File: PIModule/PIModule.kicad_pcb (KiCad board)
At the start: 2 copper layers, 56 x 60 mm, 27 parts, among them J1 SigIn, J2 HVOut, J3 Heater, J4 HeaterOut, J5 HV, J6 SigOut, J7 NFB, J8 PresencePot, U1 ECC83

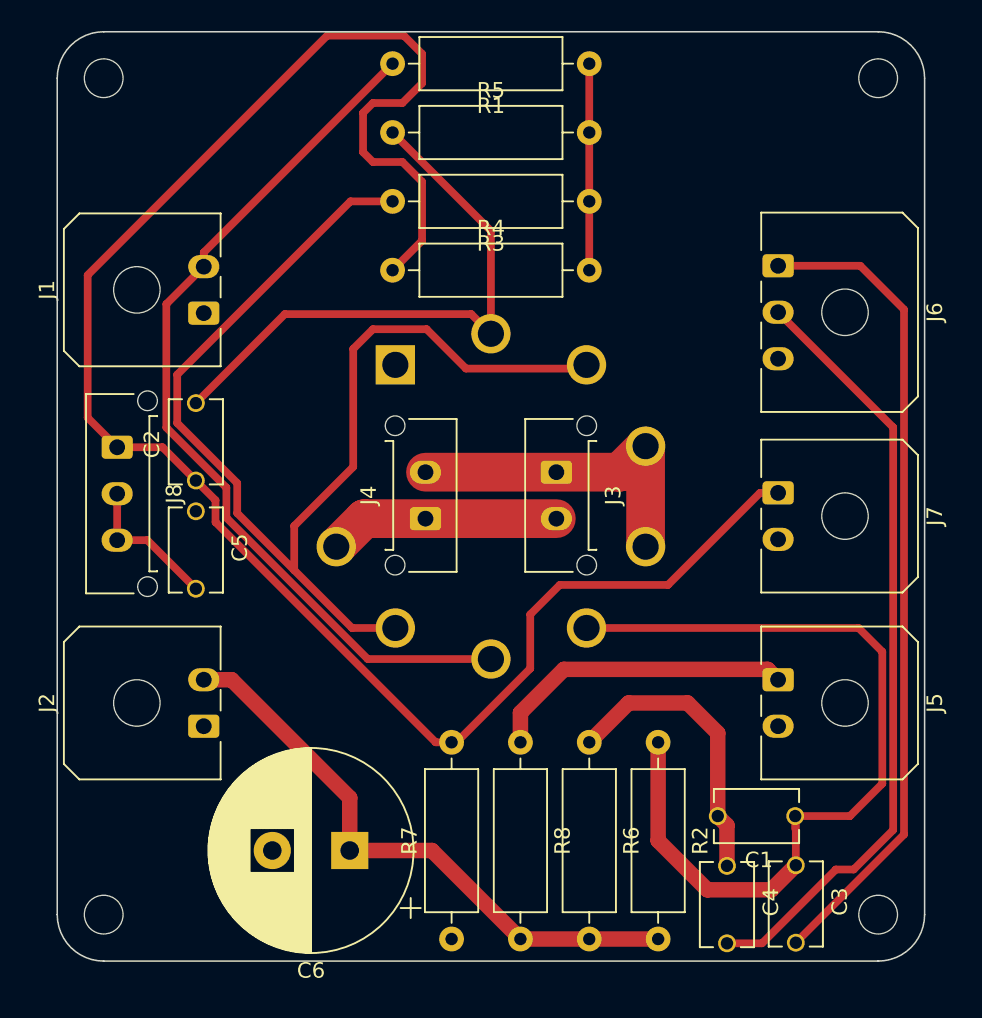
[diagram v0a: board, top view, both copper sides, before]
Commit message: Reroute phase inverter
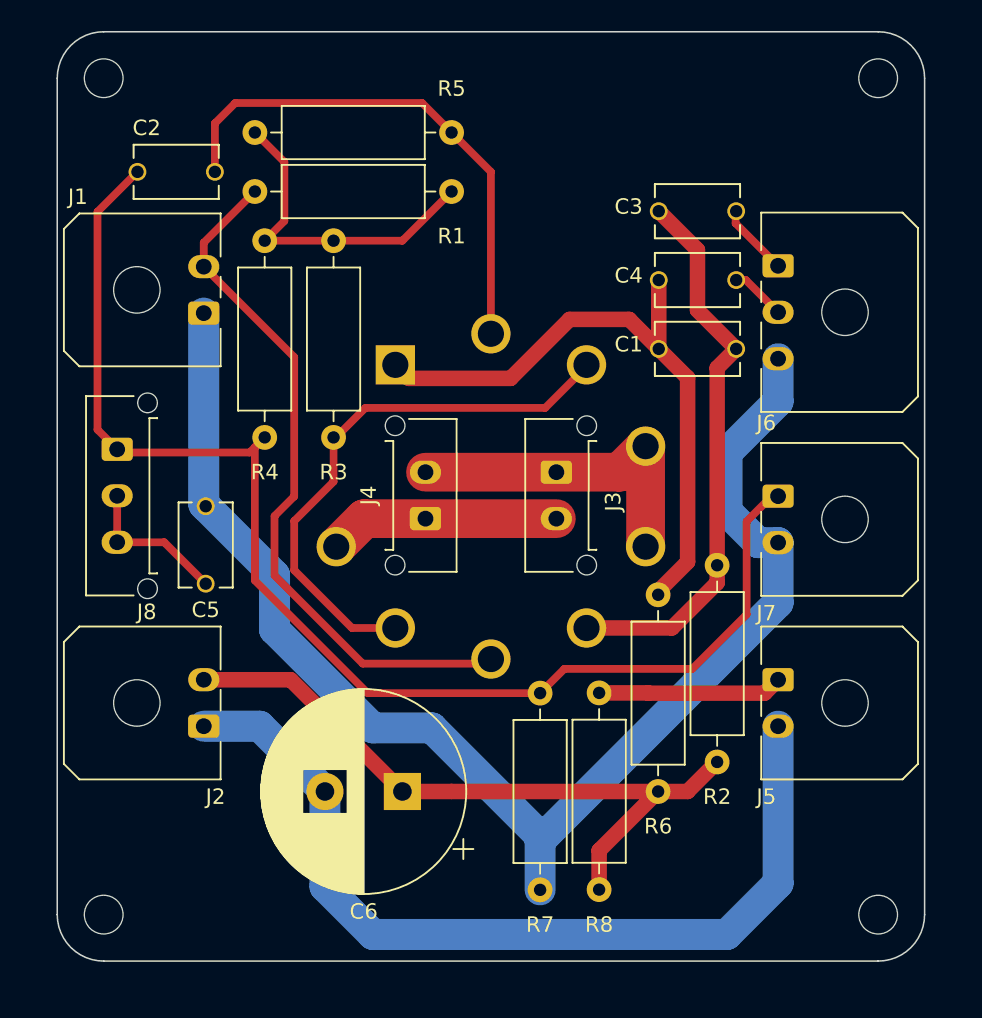
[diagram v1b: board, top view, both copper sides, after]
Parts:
- moved C3 45.2 mm to (172.7, 68.2), turned to 0 degrees
- moved C4 40.4 mm to (172.7, 72.7), turned to 0 degrees
- moved C1 30.4 mm to (172.7, 77.1)
- moved C2 17.5 mm to (139.1, 65.7), turned to 0 degrees
- moved R3 16.7 mm to (149.2, 70.1), turned to -90 degrees
- moved R4 13.6 mm to (144.8, 82.8), turned to 90 degrees
- moved R1 12.1 mm to (156.8, 67.0)
- moved R2 12.0 mm to (174.0, 91.1)
- moved R6 10.5 mm to (170.2, 93.0)
- moved R7 6.54 mm to (162.6, 112.1)
- moved R8 6.00 mm to (166.4, 99.3)
- moved C6 5.11 mm to (153.7, 105.7)
- moved R5 3.81 mm to (156.8, 63.2), turned to 180 degrees
- moved C5 0.71 mm to (141.0, 89.8)
- moved J7 0.21 mm to (177.9, 86.6)
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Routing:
- net GND: track 0.00 -> 89.4 mm
- net GND1: track 0.00 -> 57.8 mm
- net Net-(J6-Pin_1): track 53.1 -> 4.66 mm
- net Net-(J6-Pin_2): track 50.3 -> 3.57 mm
- net Net-(U1A-K): track 74.9 -> 35.8 mm
- net Net-(J7-Pin_1): track 120.9 -> 84.6 mm
- net Net-(U1B-A): track 19.0 -> 41.6 mm
- net Net-(U1A-A): track 56.3 -> 36.2 mm
- net Net-(J1-Pin_2): track 57.8 -> 45.5 mm
- net Net-(R1-Pad1): track 13.3 -> 21.7 mm
- net Net-(J5-Pin_1): track 20.0 -> 11.9 mm
- net HT: track 38.3 -> 44.8 mm
- net Net-(U1B-G): track 37.6 -> 33.8 mm

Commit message: Change connector footprints to contain 3D models. Make necessary PCB modifications to address errors found in the design
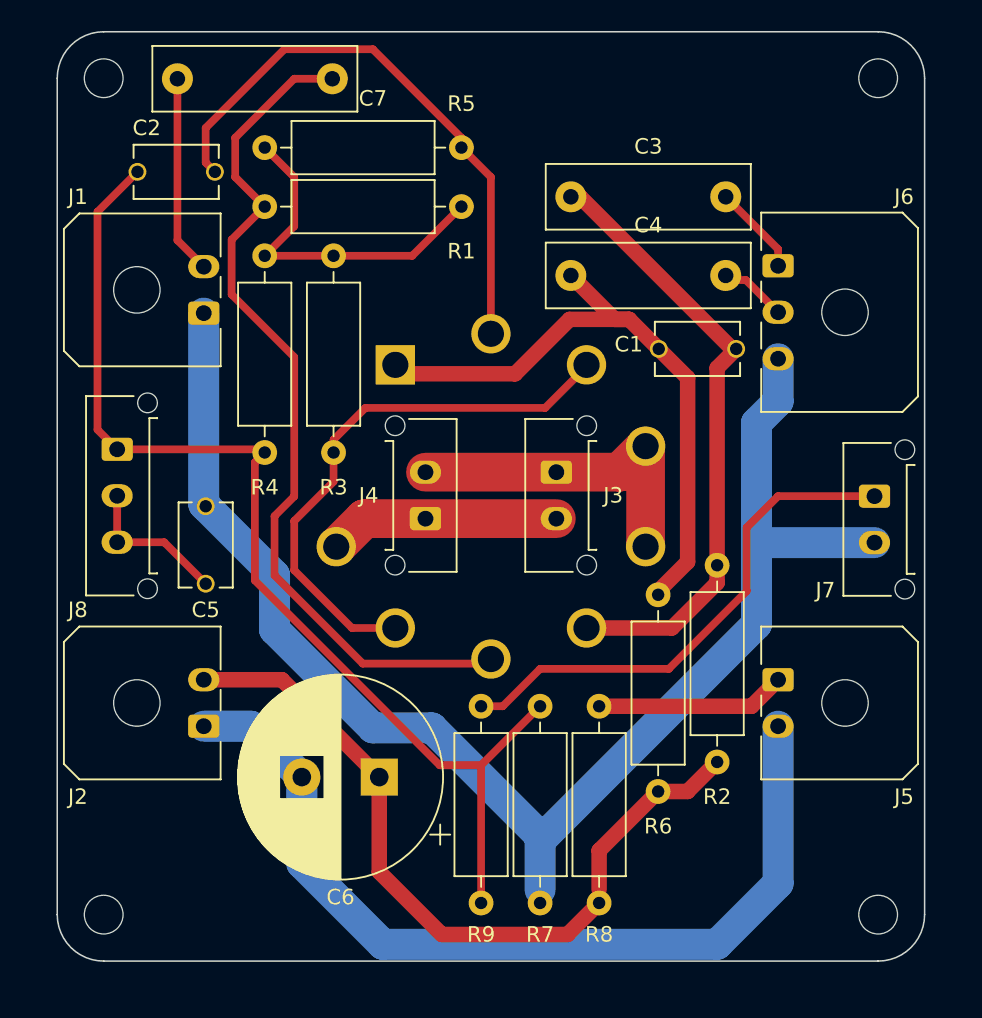
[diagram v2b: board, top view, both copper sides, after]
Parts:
- added C7: 0.022uF, Capacitor_THT:C_Rect_L13.0mm_W4.0mm_P10.00mm_FKS3_FKP3_MKS4, F.Cu at (139.1, 59.7)
- added R9: 100K, Resistor_THT:R_Axial_DIN0309_L9.0mm_D3.2mm_P12.70mm_Horizontal, F.Cu at (158.8, 112.9)
- C3, C4: footprint CustomFootprints:FG26 Cap -> Capacitor_THT:C_Rect_L13.0mm_W4.0mm_P10.00mm_FKS3_FKP3_MKS4
- J1, J2, J5: footprint Connector_Molex:Molex_Micro-Fit_3.0_43650-0200_1x02_P3.00mm_Horizontal -> CustomFootprints:Molex_Micro-Fit_3.0_43650-0200_1x02_P3.00mm_Horizontal
- J3, J4: footprint Connector_Molex:Molex_Micro-Fit_3.0_43650-0215_1x02_P3.00mm_Vertical -> CustomFootprints:Molex_Micro-Fit_3.0_43650-0215_1x02_P3.00mm_Vertical
- J6: footprint Connector_Molex:Molex_Micro-Fit_3.0_43650-0300_1x03_P3.00mm_Horizontal -> CustomFootprints:Molex_Micro-Fit_3.0_43650-0300_1x03_P3.00mm_Horizontal
- J7: footprint Connector_Molex:Molex_Micro-Fit_3.0_43650-0200_1x02_P3.00mm_Horizontal -> CustomFootprints:Molex_Micro-Fit_3.0_43650-0215_1x02_P3.00mm_Vertical
- J8: footprint Connector_Molex:Molex_Micro-Fit_3.0_43650-0315_1x03_P3.00mm_Vertical -> CustomFootprints:Molex_Micro-Fit_3.0_43650-0315_1x03_P3.00mm_Vertical
- moved C3 8.23 mm to (164.5, 67.3)
- moved C4 8.18 mm to (164.5, 72.4)
- moved J7 6.22 mm to (184.2, 86.6)
- moved C6 1.76 mm to (152.2, 104.8)
- moved R5 1.16 mm to (157.5, 64.1)
- moved R1 1.16 mm to (157.5, 67.9)
- moved R3 0.98 mm to (149.2, 71.1)
- moved R4 0.97 mm to (144.8, 83.8)
- moved R8 0.86 mm to (166.4, 100.2)
- moved R7 0.85 mm to (162.6, 112.9)
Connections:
- C2 pad 1: Net-(J7-Pin_1) -> Net-(J8-Pin_1)
- J8 pad 1: Net-(J7-Pin_1) -> Net-(J8-Pin_1)
- R1 pad 2: Net-(J1-Pin_2) -> Net-(U1A-G)
- R4 pad 1: Net-(J7-Pin_1) -> Net-(J8-Pin_1)
- R7 pad 2: Net-(J7-Pin_1) -> Net-(J8-Pin_1)
- U1 pad 7: Net-(J1-Pin_2) -> Net-(U1A-G)
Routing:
- net Net-(J8-Pin_1): track 0.00 -> 71.8 mm
- net Net-(U1A-G): track 0.00 -> 56.4 mm
- net Net-(J7-Pin_1): track 84.6 -> 33.4 mm
- net Net-(J1-Pin_2): track 45.5 -> 12.8 mm
- net HT: track 44.8 -> 49.3 mm
- net GND: track 89.4 -> 93.6 mm
- net Net-(U1A-A): track 36.2 -> 40.0 mm
- net Net-(U1B-G): track 33.8 -> 37.5 mm
- net Net-(J6-Pin_1): track 4.66 -> 5.86 mm
- net Net-(R1-Pad1): track 21.7 -> 22.6 mm

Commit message: Standardized hole size across all boards
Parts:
- removed the REF** at (134.4, 113.7)
- removed the REF** at (184.4, 113.7)
- removed the REF** at (184.4, 59.7)
- removed the REF** at (134.4, 59.7)
- added REF**: MountingHole_2.7mm_M2.5, MountingHole:MountingHole_2.7mm_M2.5, F.Cu at (184.4, 113.7)
- added REF**: MountingHole_2.7mm_M2.5, MountingHole:MountingHole_2.7mm_M2.5, F.Cu at (184.4, 59.7)
- added REF**: MountingHole_2.7mm_M2.5, MountingHole:MountingHole_2.7mm_M2.5, F.Cu at (134.4, 113.7)
- added REF**: MountingHole_2.7mm_M2.5, MountingHole:MountingHole_2.7mm_M2.5, F.Cu at (134.4, 59.7)
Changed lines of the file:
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@@
     )
     (pad_to_mask_clearance 0)
+    (grid_origin 159.385 86.655)
     (pcbplotparams
       (layerselection 0x00010fc_ffffffff)
@@
         (effects (font (size 1 1) (thickness 0.15)))
     )
-    (fp_text value "SigOut" (at 3 3.22 -90) (layer "F.Fab")
+    (fp_text value "SigOut" (at 8.245 -5.59) (layer "F.Fab")
         (effects (font (size 1 1) (thickness 0.15)))
     )
@@
     )
   )
-  (footprint "MountingHole:MountingHole_2.5mm" (layer "F.Cu")
-    (at 134.385 113.655)
-    (descr "Mounting Hole 2.5mm, no annular")
-    (tags "mounting hole 2.5mm no annular")
+  (footprint "MountingHole:MountingHole_2.7mm_M2.5" (layer "F.Cu")
+    (at 184.385 113.655)
+    (descr "Mounting Hole 2.7mm, no annular, M2.5")
+    (tags "mounting hole 2.7mm no annular m2.5")
     (attr exclude_from_pos_files exclude_from_bom)
-    (fp_text reference "REF**" (at 0 -3.5) (layer "F.SilkS") hide
-        (effects (font (size 1 1) (thickness 0.15)))
-    )
-    (fp_text value "MountingHole_2.5mm" (at 0 3.5) (layer "F.Fab") hide
+    (fp_text reference "REF**" (at 0 -3.7) (layer "F.SilkS") hide
+        (effects (font (size 1 1) (thickness 0.15)))
+    )
+    (fp_text value "MountingHole_2.7mm_M2.5" (at 0 3.7) (layer "F.Fab") hide
         (effects (font (size 1 1) (thickness 0.15)))
     )
@@
         (effects (font (size 1 1) (thickness 0.15)))
     )
-    (fp_circle (center 0 0) (end 2.5 0)
+    (fp_circle (center 0 0) (end 2.7 0)
       (stroke (width 0.15) (type solid)) (fill none) (layer "Cmts.User"))
-    (fp_circle (center 0 0) (end 2.75 0)
+    (fp_circle (center 0 0) (end 2.95 0)
       (stroke (width 0.05) (type solid)) (fill none) (layer "F.CrtYd"))
-    (pad "" np_thru_hole circle (at 0 0) (size 2.5 2.5) (drill 2.5) (layers "F&B.Cu" "*.Mask"))
+    (pad "" np_thru_hole circle (at 0 0) (size 2.7 2.7) (drill 2.7) (layers "*.Cu" "*.Mask"))
   )
   (footprint "Resistor_THT:R_Axial_DIN0309_L9.0mm_D3.2mm_P12.70mm_Horizontal" (layer "F.Cu")
@@
     )
   )
-  (footprint "MountingHole:MountingHole_2.5mm" (layer "F.Cu")
-    (at 184.385 113.655)
-    (descr "Mounting Hole 2.5mm, no annular")
-    (tags "mounting hole 2.5mm no annular")
-    (attr exclude_from_pos_files exclude_from_bom)
-    (fp_text reference "REF**" (at 0 -3.5) (layer "F.SilkS") hide
-        (effects (font (size 1 1) (thickness 0.15)))
-    )
-    (fp_text value "MountingHole_2.5mm" (at 0 3.5) (layer "F.Fab") hide
-        (effects (font (size 1 1) (thickness 0.15)))
-    )
-    (fp_text user "${REFERENCE}" (at 0 0) (layer "F.Fab")
-        (effects (font (size 1 1) (thickness 0.15)))
-    )
-    (fp_circle (center 0 0) (end 2.5 0)
-      (stroke (width 0.15) (type solid)) (fill none) (layer "Cmts.User"))
-    (fp_circle (center 0 0) (end 2.75 0)
-      (stroke (width 0.05) (type solid)) (fill none) (layer "F.CrtYd"))
-    (pad "" np_thru_hole circle (at 0 0) (size 2.5 2.5) (drill 2.5) (layers "F&B.Cu" "*.Mask"))
-  )
-  (footprint "MountingHole:MountingHole_2.5mm" (layer "F.Cu")
-    (at 184.385 59.655)
-    (descr "Mounting Hole 2.5mm, no annular")
-    (tags "mounting hole 2.5mm no annular")
-    (attr exclude_from_pos_files exclude_from_bom)
-    (fp_text reference "REF**" (at 0 -3.5) (layer "F.SilkS") hide
-        (effects (font (size 1 1) (thickness 0.15)))
-    )
-    (fp_text value "MountingHole_2.5mm" (at 0 3.5) (layer "F.Fab") hide
-        (effects (font (size 1 1) (thickness 0.15)))
-    )
-    (fp_text user "${REFERENCE}" (at 0 0) (layer "F.Fab")
-        (effects (font (size 1 1) (thickness 0.15)))
-    )
-    (fp_circle (center 0 0) (end 2.5 0)
-      (stroke (width 0.15) (type solid)) (fill none) (layer "Cmts.User"))
-    (fp_circle (center 0 0) (end 2.75 0)
-      (stroke (width 0.05) (type solid)) (fill none) (layer "F.CrtYd"))
-    (pad "" np_thru_hole circle (at 0 0) (size 2.5 2.5) (drill 2.5) (layers "F&B.Cu" "*.Mask"))
-  )
   (footprint "Capacitor_THT:C_Rect_L13.0mm_W4.0mm_P10.00mm_FKS3_FKP3_MKS4" (layer "F.Cu")
     (at 164.545 72.39)
@@
     )
   )
+  (footprint "MountingHole:MountingHole_2.7mm_M2.5" (layer "F.Cu")
+    (at 184.385 59.655)
+    (descr "Mounting Hole 2.7mm, no annular, M2.5")
+    (tags "mounting hole 2.7mm no annular m2.5")
+    (attr exclude_from_pos_files exclude_from_bom)
+    (fp_text reference "REF**" (at 0 -3.7) (layer "F.SilkS") hide
+        (effects (font (size 1 1) (thickness 0.15)))
+    )
+    (fp_text value "MountingHole_2.7mm_M2.5" (at 0 3.7) (layer "F.Fab") hide
+        (effects (font (size 1 1) (thickness 0.15)))
+    )
+    (fp_text user "${REFERENCE}" (at 0 0) (layer "F.Fab")
+        (effects (font (size 1 1) (thickness 0.15)))
+    )
+    (fp_circle (center 0 0) (end 2.7 0)
+      (stroke (width 0.15) (type solid)) (fill none) (layer "Cmts.User"))
+    (fp_circle (center 0 0) (end 2.95 0)
+      (stroke (width 0.05) (type solid)) (fill none) (layer "F.CrtYd"))
+    (pad "" np_thru_hole circle (at 0 0) (size 2.7 2.7) (drill 2.7) (layers "*.Cu" "*.Mask"))
+  )
+  (footprint "MountingHole:MountingHole_2.7mm_M2.5" (layer "F.Cu")
+    (at 134.385 113.655)
+    (descr "Mounting Hole 2.7mm, no annular, M2.5")
+    (tags "mounting hole 2.7mm no annular m2.5")
+    (attr exclude_from_pos_files exclude_from_bom)
+    (fp_text reference "REF**" (at 0 -3.7) (layer "F.SilkS") hide
+        (effects (font (size 1 1) (thickness 0.15)))
+    )
+    (fp_text value "MountingHole_2.7mm_M2.5" (at 0 3.7) (layer "F.Fab") hide
+        (effects (font (size 1 1) (thickness 0.15)))
+    )
+    (fp_text user "${REFERENCE}" (at 0 0) (layer "F.Fab")
+        (effects (font (size 1 1) (thickness 0.15)))
+    )
+    (fp_circle (center 0 0) (end 2.7 0)
+      (stroke (width 0.15) (type solid)) (fill none) (layer "Cmts.User"))
+    (fp_circle (center 0 0) (end 2.95 0)
+      (stroke (width 0.05) (type solid)) (fill none) (layer "F.CrtYd"))
+    (pad "" np_thru_hole circle (at 0 0) (size 2.7 2.7) (drill 2.7) (layers "*.Cu" "*.Mask"))
+  )
   (footprint "Capacitor_THT:C_Rect_L13.0mm_W4.0mm_P10.00mm_FKS3_FKP3_MKS4" (layer "F.Cu")
     (at 139.145 59.69)
@@
       (rotate (xyz 0 0 0))
     )
+  )
+  (footprint "MountingHole:MountingHole_2.7mm_M2.5" (layer "F.Cu")
+    (at 134.385 59.655)
+    (descr "Mounting Hole 2.7mm, no annular, M2.5")
+    (tags "mounting hole 2.7mm no annular m2.5")
+    (attr exclude_from_pos_files exclude_from_bom)
+    (fp_text reference "REF**" (at 0 -3.7) (layer "F.SilkS") hide
+        (effects (font (size 1 1) (thickness 0.15)))
+    )
+    (fp_text value "MountingHole_2.7mm_M2.5" (at 0 3.7) (layer "F.Fab") hide
+        (effects (font (size 1 1) (thickness 0.15)))
+    )
+    (fp_text user "${REFERENCE}" (at 0 0) (layer "F.Fab")
+        (effects (font (size 1 1) (thickness 0.15)))
+    )
+    (fp_circle (center 0 0) (end 2.7 0)
+      (stroke (width 0.15) (type solid)) (fill none) (layer "Cmts.User"))
+    (fp_circle (center 0 0) (end 2.95 0)
+      (stroke (width 0.05) (type solid)) (fill none) (layer "F.CrtYd"))
+    (pad "" np_thru_hole circle (at 0 0) (size 2.7 2.7) (drill 2.7) (layers "*.Cu" "*.Mask"))
   )
   (footprint "CustomFootprints:Molex_Micro-Fit_3.0_43650-0215_1x02_P3.00mm_Vertical" (layer "F.Cu")
@@
         (effects (font (size 1 1) (thickness 0.15)))
     )
-    (fp_text value "HV" (at 1.5 3.22 -90) (layer "F.Fab")
+    (fp_text value "HV" (at 5.65 -6.86) (layer "F.Fab")
         (effects (font (size 1 1) (thickness 0.15)))
     )
@@
     )
   )
-  (footprint "MountingHole:MountingHole_2.5mm" (layer "F.Cu")
-    (at 134.385 59.655)
-    (descr "Mounting Hole 2.5mm, no annular")
-    (tags "mounting hole 2.5mm no annular")
-    (attr exclude_from_pos_files exclude_from_bom)
-    (fp_text reference "REF**" (at 0 -3.5) (layer "F.SilkS") hide
-        (effects (font (size 1 1) (thickness 0.15)))
-    )
-    (fp_text value "MountingHole_2.5mm" (at 0 3.5) (layer "F.Fab") hide
-        (effects (font (size 1 1) (thickness 0.15)))
-    )
-    (fp_text user "${REFERENCE}" (at 0 0) (layer "F.Fab")
-        (effects (font (size 1 1) (thickness 0.15)))
-    )
-    (fp_circle (center 0 0) (end 2.5 0)
-      (stroke (width 0.15) (type solid)) (fill none) (layer "Cmts.User"))
-    (fp_circle (center 0 0) (end 2.75 0)
-      (stroke (width 0.05) (type solid)) (fill none) (layer "F.CrtYd"))
-    (pad "" np_thru_hole circle (at 0 0) (size 2.5 2.5) (drill 2.5) (layers "F&B.Cu" "*.Mask"))
-  )
   (footprint "CustomFootprints:BELTON_VT9-PT" (layer "B.Cu")
